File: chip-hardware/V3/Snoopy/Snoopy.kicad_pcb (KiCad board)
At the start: 2 copper layers, 49.8 x 29.2 mm, 13 parts, among them J1 Screw_Terminal_01x02, J2 KLDX-0202-B, J3 501461-0491, J4 Conn_01x02, U1 INA260, U2 TLV70033_SOT23-5, U3 ESP32-WROOM-32

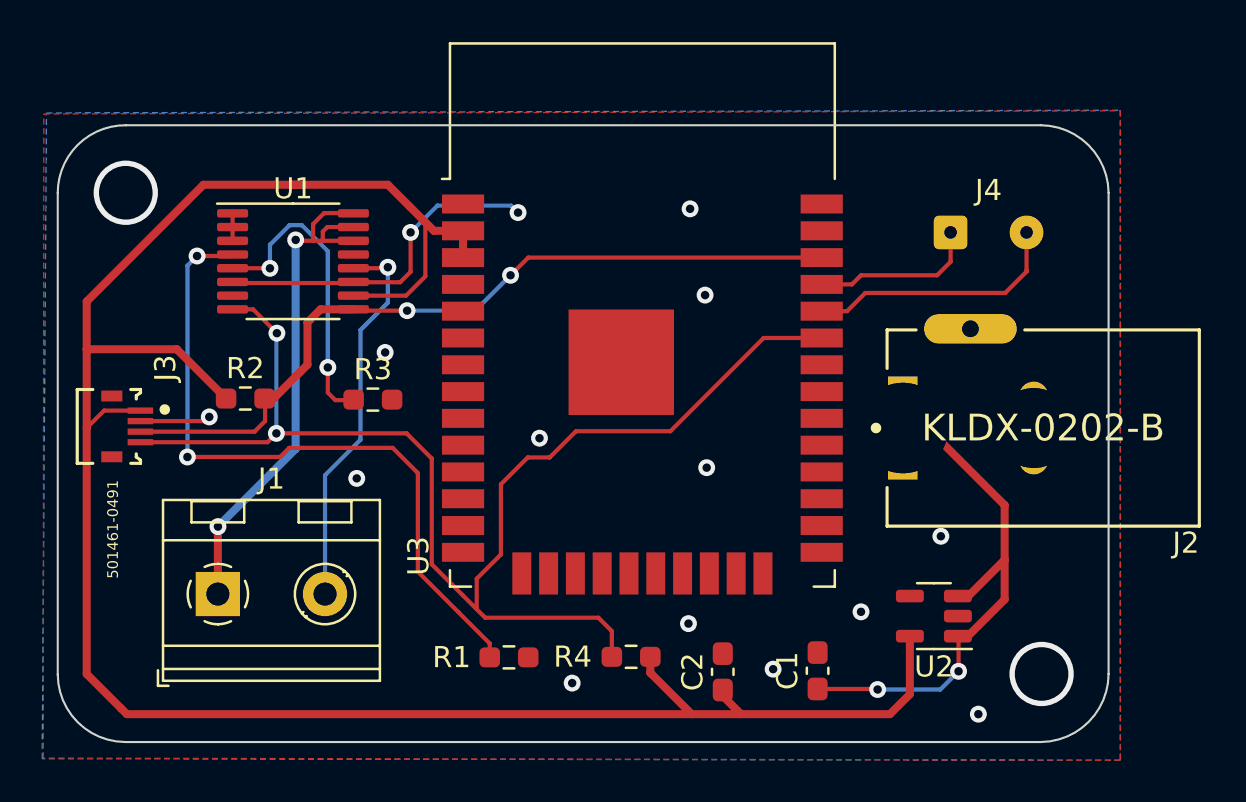
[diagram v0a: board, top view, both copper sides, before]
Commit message: Had to manually go in and modify the drill holes. not sure why they were like that but I think i fixed them. Gonna get the a-okay from chris first before sending them in
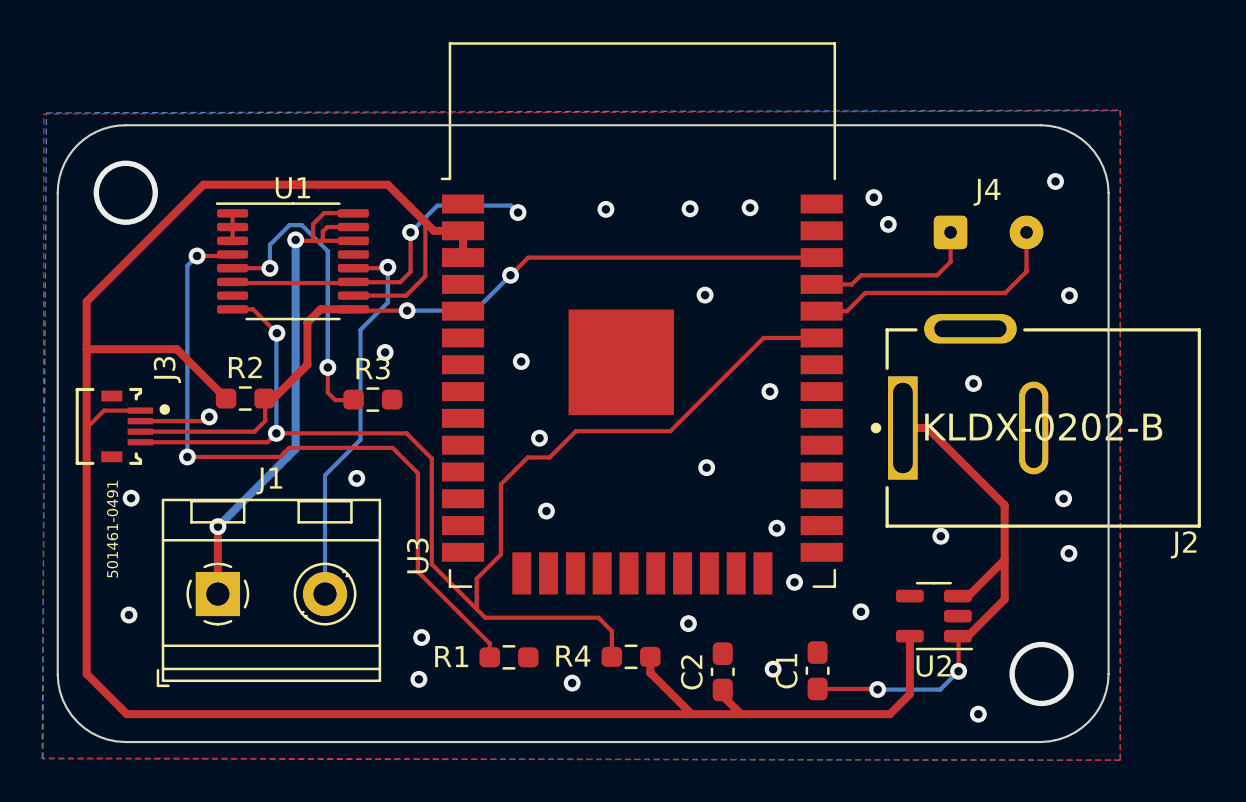
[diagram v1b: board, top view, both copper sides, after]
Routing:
- net GND: vias 15 -> 33
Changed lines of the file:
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@@
     (fp_line (start -7.4 -4.65) (end 7.4 -4.65) (layer "F.Fab") (width 0.15))
     (fp_line (start 7.4 4.65) (end -7.4 4.65) (layer "F.Fab") (width 0.15))
-    (pad "1" thru_hole rect locked (at 6.65 0 180) (size 1.4 4.899999) (drill oval 4.3) (layers *.Cu)
+    (pad "1" thru_hole rect locked (at 6.65 0 180) (size 1.4 4.899999) (drill oval 0.938 4.3) (layers *.Cu *.Mask)
       (net 1 "Net-(C1-Pad1)") (pinfunction "1") (pintype "power_in"))
-    (pad "2" thru_hole roundrect locked (at 0.45 0 180) (size 1.4 4.4) (drill oval 3.8) (layers *.Cu) (roundrect_rratio 0.5)
+    (pad "2" thru_hole roundrect locked (at 0.45 0 180) (size 1.4 4.4) (drill oval 0.8118 3.8) (layers *.Cu *.Mask) (roundrect_rratio 0.5)
       (net 2 "GND") (pinfunction "2") (pintype "power_in"))
-    (pad "3" thru_hole roundrect locked (at 3.45 4.7 180) (size 4.4 1.4) (drill oval 0.8) (layers *.Cu) (roundrect_rratio 0.5)
+    (pad "3" thru_hole roundrect locked (at 3.45 4.7 180) (size 4.4 1.4) (drill oval 3.428 0.8) (layers *.Cu *.Mask) (roundrect_rratio 0.5)
       (net 2 "GND") (pinfunction "3") (pintype "power_in"))
     (model "eec.models/Kycon_-_KLDX-0202-B.step"
@@
   (segment (start 121.0135 76.7334) (end 120.9979 76.7178) (width 0.2) (layer "F.Cu") (net 2))
   (via (at 136.9568 73.2536) (size 0.8) (drill 0.4) (layers "F.Cu" "B.Cu") (free) (net 2))
+  (via (at 110.363 92.5068) (size 0.8) (drill 0.4) (layers "F.Cu" "B.Cu") (free) (net 2))
   (via (at 136.8806 92.9132) (size 0.8) (drill 0.4) (layers "F.Cu" "B.Cu") (free) (net 2))
   (via (at 140.8938 95.0722) (size 0.8) (drill 0.4) (layers "F.Cu" "B.Cu") (free) (net 2))
@@
   (via (at 129.8194 84.1248) (size 0.8) (drill 0.4) (layers "F.Cu" "B.Cu") (free) (net 2))
   (via (at 123.7097 74.3712) (size 0.8) (drill 0.4) (layers "F.Cu" "B.Cu") (free) (net 2))
+  (via (at 124.2314 93.5736) (size 0.8) (drill 0.4) (layers "F.Cu" "B.Cu") (free) (net 2))
   (via (at 122.5042 80.0608) (size 0.8) (drill 0.4) (layers "F.Cu" "B.Cu") (free) (net 2))
   (via (at 137.668 77.343) (size 0.8) (drill 0.4) (layers "F.Cu" "B.Cu") (free) (net 2))
+  (via (at 154.2796 71.9582) (size 0.8) (drill 0.4) (layers "F.Cu" "B.Cu") (free) (net 2))
+  (via (at 140.7414 81.915) (size 0.8) (drill 0.4) (layers "F.Cu" "B.Cu") (free) (net 2))
   (via (at 137.7442 85.5218) (size 0.8) (drill 0.4) (layers "F.Cu" "B.Cu") (free) (net 2))
+  (via (at 154.9146 89.5858) (size 0.8) (drill 0.4) (layers "F.Cu" "B.Cu") (free) (net 2))
+  (via (at 141.0716 88.392) (size 0.8) (drill 0.4) (layers "F.Cu" "B.Cu") (free) (net 2))
   (via (at 114.166844 83.115923) (size 0.8) (drill 0.4) (layers "F.Cu" "B.Cu") (net 2))
   (via (at 128.8034 73.4314) (size 0.8) (drill 0.4) (layers "F.Cu" "B.Cu") (free) (net 2))
   (via (at 145.0594 92.3544) (size 0.8) (drill 0.4) (layers "F.Cu" "B.Cu") (free) (net 2))
+  (via (at 139.8016 73.2028) (size 0.8) (drill 0.4) (layers "F.Cu" "B.Cu") (free) (net 2))
   (via (at 148.844 88.773) (size 0.8) (drill 0.4) (layers "F.Cu" "B.Cu") (free) (net 2))
   (via (at 131.3688 95.7326) (size 0.8) (drill 0.4) (layers "F.Cu" "B.Cu") (free) (net 2))
+  (via (at 141.9098 90.9574) (size 0.8) (drill 0.4) (layers "F.Cu" "B.Cu") (free) (net 2))
+  (via (at 154.6606 86.995) (size 0.8) (drill 0.4) (layers "F.Cu" "B.Cu") (free) (net 2))
+  (via (at 146.3548 73.9902) (size 0.8) (drill 0.4) (layers "F.Cu" "B.Cu") (free) (net 2))
+  (via (at 128.9558 80.4926) (size 0.8) (drill 0.4) (layers "F.Cu" "B.Cu") (free) (net 2))
+  (via (at 154.94 77.3684) (size 0.8) (drill 0.4) (layers "F.Cu" "B.Cu") (free) (net 2))
+  (via (at 124.1044 95.5548) (size 0.8) (drill 0.4) (layers "F.Cu" "B.Cu") (free) (net 2))
+  (via (at 145.669 72.7202) (size 0.8) (drill 0.4) (layers "F.Cu" "B.Cu") (free) (net 2))
+  (via (at 132.969 73.279) (size 0.8) (drill 0.4) (layers "F.Cu" "B.Cu") (free) (net 2))
+  (via (at 110.4646 86.9696) (size 0.8) (drill 0.4) (layers "F.Cu" "B.Cu") (free) (net 2))
+  (via (at 150.3934 81.534) (size 0.8) (drill 0.4) (layers "F.Cu" "B.Cu") (free) (net 2))
   (via (at 150.622 97.2058) (size 0.8) (drill 0.4) (layers "F.Cu" "B.Cu") (free) (net 2))
+  (via (at 130.1496 87.5792) (size 0.8) (drill 0.4) (layers "F.Cu" "B.Cu") (free) (net 2))
   (segment (start 128.4732 73.1012) (end 128.8034 73.4314) (width 0.2) (layer "B.Cu") (net 2))
   (segment (start 124.9797 73.1012) (end 128.4732 73.1012) (width 0.2) (layer "B.Cu") (net 2))

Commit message: Created groud planes and fixed power jack issues. Issued new gerbers for both relevant files
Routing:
- net GND: vias 33 -> 35
- net (no net): vias 2 -> 0
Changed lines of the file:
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@@
   (gr_arc (start 156.7942 95.3008) (mid 155.852841 97.567353) (end 153.5938 98.5266) (layer "Edge.Cuts") (width 0.1))
   (gr_line (start 153.5938 98.5266) (end 110.1852 98.5266) (layer "Edge.Cuts") (width 0.1))
-  (via (at 153.6192 95.3008) (size 3.048) (drill 2.54) (layers "F.Cu" "B.Cu") (free) (net 0))
-  (via (at 110.2106 72.4916) (size 3.048) (drill 2.54) (layers "F.Cu" "B.Cu") (free) (net 0))
   (segment (start 151.8666 89.8906) (end 151.8666 91.768503) (width 0.381) (layer "F.Cu") (net 1))
   (segment (start 149.6822 95.1738) (end 149.6822 93.5385) (width 0.2) (layer "F.Cu") (net 1))
@@
   (via (at 121.158 86.0298) (size 0.8) (drill 0.4) (layers "F.Cu" "B.Cu") (free) (net 2))
   (via (at 129.8194 84.1248) (size 0.8) (drill 0.4) (layers "F.Cu" "B.Cu") (free) (net 2))
+  (via (at 153.6192 95.3008) (size 3.048) (drill 2.54) (layers "F.Cu" "B.Cu") (free) (net 2))
   (via (at 123.7097 74.3712) (size 0.8) (drill 0.4) (layers "F.Cu" "B.Cu") (free) (net 2))
   (via (at 124.2314 93.5736) (size 0.8) (drill 0.4) (layers "F.Cu" "B.Cu") (free) (net 2))
@@
   (via (at 150.622 97.2058) (size 0.8) (drill 0.4) (layers "F.Cu" "B.Cu") (free) (net 2))
   (via (at 130.1496 87.5792) (size 0.8) (drill 0.4) (layers "F.Cu" "B.Cu") (free) (net 2))
+  (via (at 110.2106 72.4916) (size 3.048) (drill 2.54) (layers "F.Cu" "B.Cu") (free) (net 2))
   (segment (start 128.4732 73.1012) (end 128.8034 73.4314) (width 0.2) (layer "B.Cu") (net 2))
   (segment (start 124.9797 73.1012) (end 128.4732 73.1012) (width 0.2) (layer "B.Cu") (net 2))

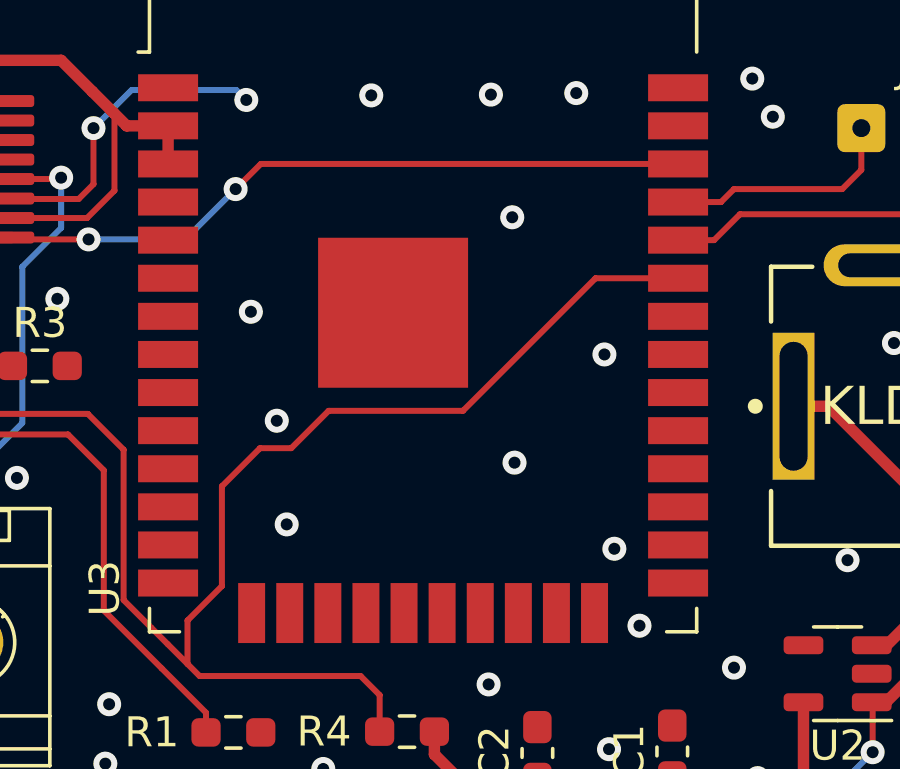
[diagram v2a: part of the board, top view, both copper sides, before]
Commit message: some hardware changes and the addition of the backend into the system
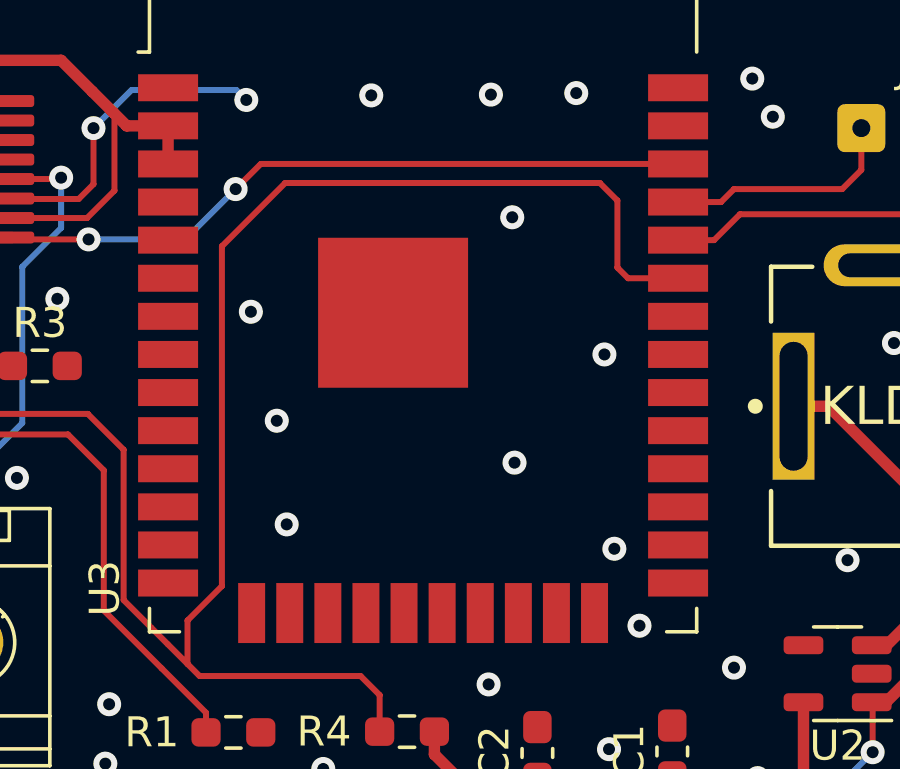
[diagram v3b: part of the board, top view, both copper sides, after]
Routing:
- net /SDA: track 62.4 -> 71.0 mm
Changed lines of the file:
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@@
   (segment (start 117.348 83.8962) (end 123.5202 83.8962) (width 0.2) (layer "F.Cu") (net 8))
   (segment (start 126.843589 90.783611) (end 127.9906 89.6366) (width 0.2) (layer "F.Cu") (net 8))
+  (segment (start 141.1732 76.7842) (end 141.1732 79.0194) (width 0.2) (layer "F.Cu") (net 8))
   (segment (start 117.3734 79.1464) (end 116.2448 78.0178) (width 0.2) (layer "F.Cu") (net 8))
-  (segment (start 127.9906 86.3092) (end 129.2606 85.0392) (width 0.2) (layer "F.Cu") (net 8))
   (segment (start 126.183189 91.571011) (end 126.843589 92.231411) (width 0.2) (layer "F.Cu") (net 8))
   (segment (start 126.843589 92.231411) (end 127.245978 92.6338) (width 0.2) (layer "F.Cu") (net 8))
-  (segment (start 140.445222 79.375) (end 143.1962 79.375) (width 0.2) (layer "F.Cu") (net 8))
   (segment (start 133.2484 93.2688) (end 133.2484 94.488) (width 0.2) (layer "F.Cu") (net 8))
-  (segment (start 129.2606 85.0392) (end 130.302 85.0392) (width 0.2) (layer "F.Cu") (net 8))
-  (segment (start 136.025622 83.7946) (end 140.445222 79.375) (width 0.2) (layer "F.Cu") (net 8))
+  (segment (start 126.843589 92.231411) (end 126.843589 90.783611) (width 0.2) (layer "F.Cu") (net 8))
+  (segment (start 127.9906 78.3082) (end 130.0988 76.2) (width 0.2) (layer "F.Cu") (net 8))
   (segment (start 116.928199 84.316001) (end 117.348 83.8962) (width 0.2) (layer "F.Cu") (net 8))
   (segment (start 124.714 90.101822) (end 125.637089 91.024911) (width 0.2) (layer "F.Cu") (net 8))
-  (segment (start 130.302 85.0392) (end 131.5466 83.7946) (width 0.2) (layer "F.Cu") (net 8))
-  (segment (start 127.9906 89.6366) (end 127.9906 86.3092) (width 0.2) (layer "F.Cu") (net 8))
+  (segment (start 127.9906 89.6366) (end 127.9906 78.3082) (width 0.2) (layer "F.Cu") (net 8))
   (segment (start 132.6134 92.6338) (end 133.2484 93.2688) (width 0.2) (layer "F.Cu") (net 8))
-  (segment (start 131.5466 83.7946) (end 136.025622 83.7946) (width 0.2) (layer "F.Cu") (net 8))
+  (segment (start 140.589 76.2) (end 141.1732 76.7842) (width 0.2) (layer "F.Cu") (net 8))
+  (segment (start 130.0988 76.2) (end 140.589 76.2) (width 0.2) (layer "F.Cu") (net 8))
   (segment (start 125.637089 91.024911) (end 126.183189 91.571011) (width 0.2) (layer "F.Cu") (net 8))
   (segment (start 124.714 85.09) (end 124.714 90.101822) (width 0.2) (layer "F.Cu") (net 8))
-  (segment (start 126.843589 92.231411) (end 126.843589 90.783611) (width 0.2) (layer "F.Cu") (net 8))
+  (segment (start 141.5288 79.375) (end 143.1962 79.375) (width 0.2) (layer "F.Cu") (net 8))
   (segment (start 110.903202 84.316001) (end 116.928199 84.316001) (width 0.2) (layer "F.Cu") (net 8))
   (segment (start 123.5202 83.8962) (end 124.714 85.09) (width 0.2) (layer "F.Cu") (net 8))
+  (segment (start 141.1732 79.0194) (end 141.5288 79.375) (width 0.2) (layer "F.Cu") (net 8))
   (segment (start 116.2448 78.0178) (end 115.2729 78.0178) (width 0.2) (layer "F.Cu") (net 8))
   (via (at 117.348 83.8962) (size 0.8) (drill 0.4) (layers "F.Cu" "B.Cu") (net 8))
